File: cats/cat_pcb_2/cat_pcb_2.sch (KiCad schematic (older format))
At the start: 6 parts, among them SW1 SMT_SPDT

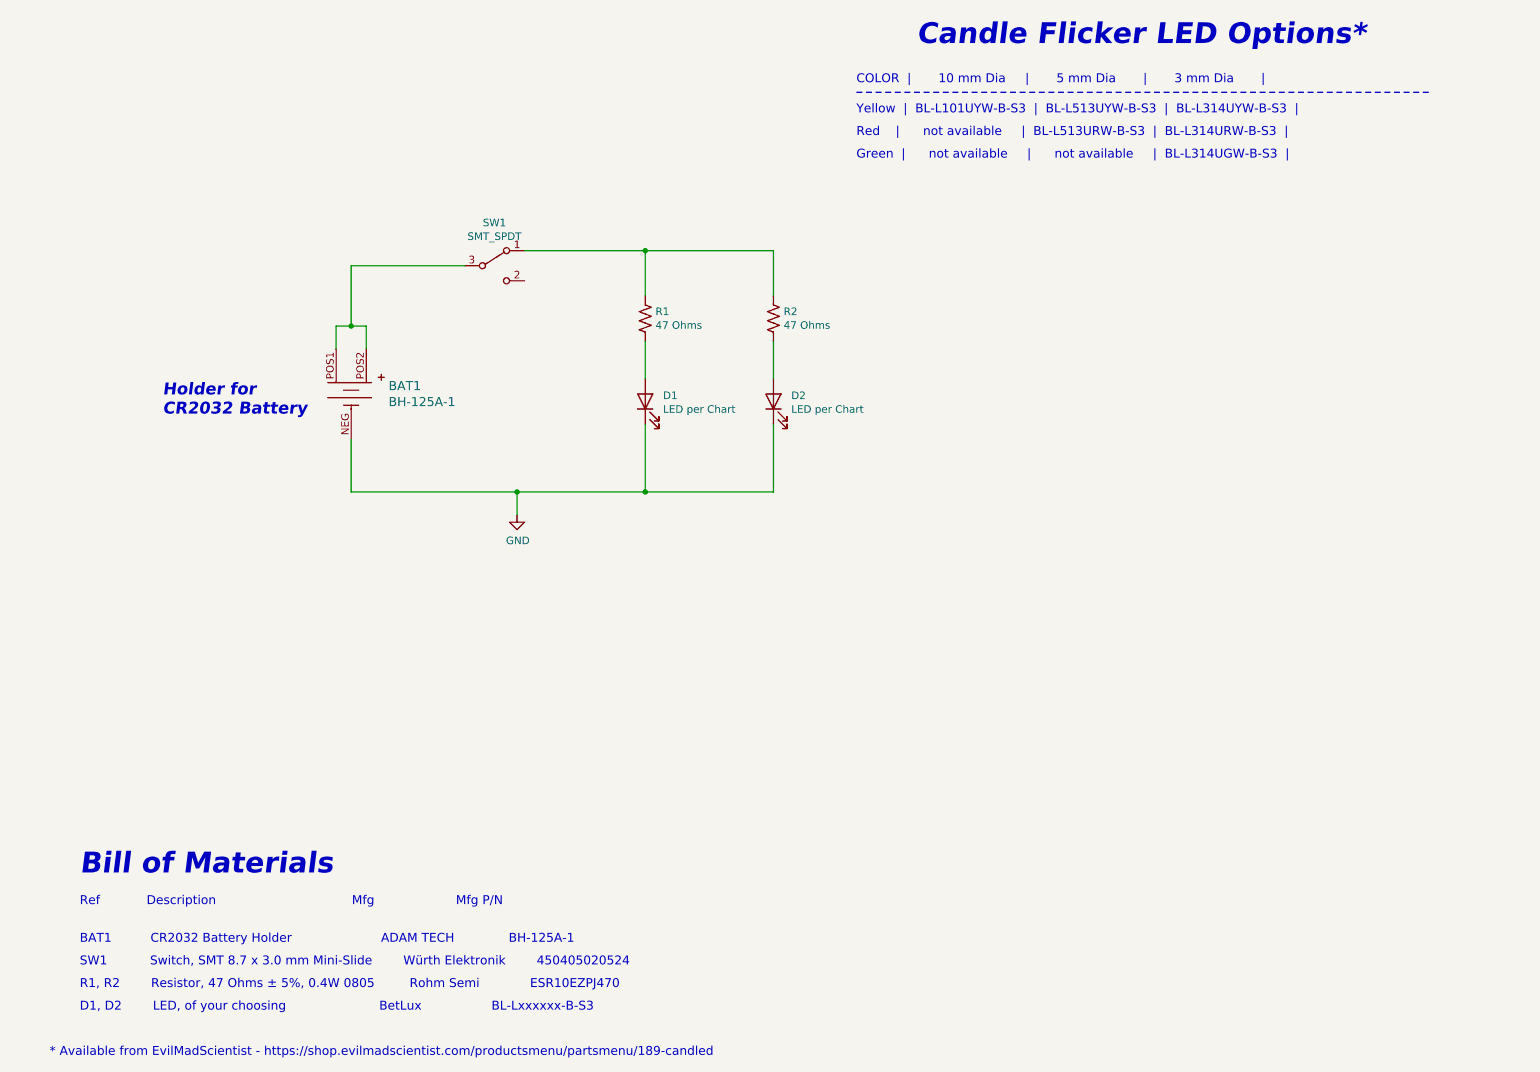
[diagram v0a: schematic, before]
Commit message: Updating all PCBS, etc.
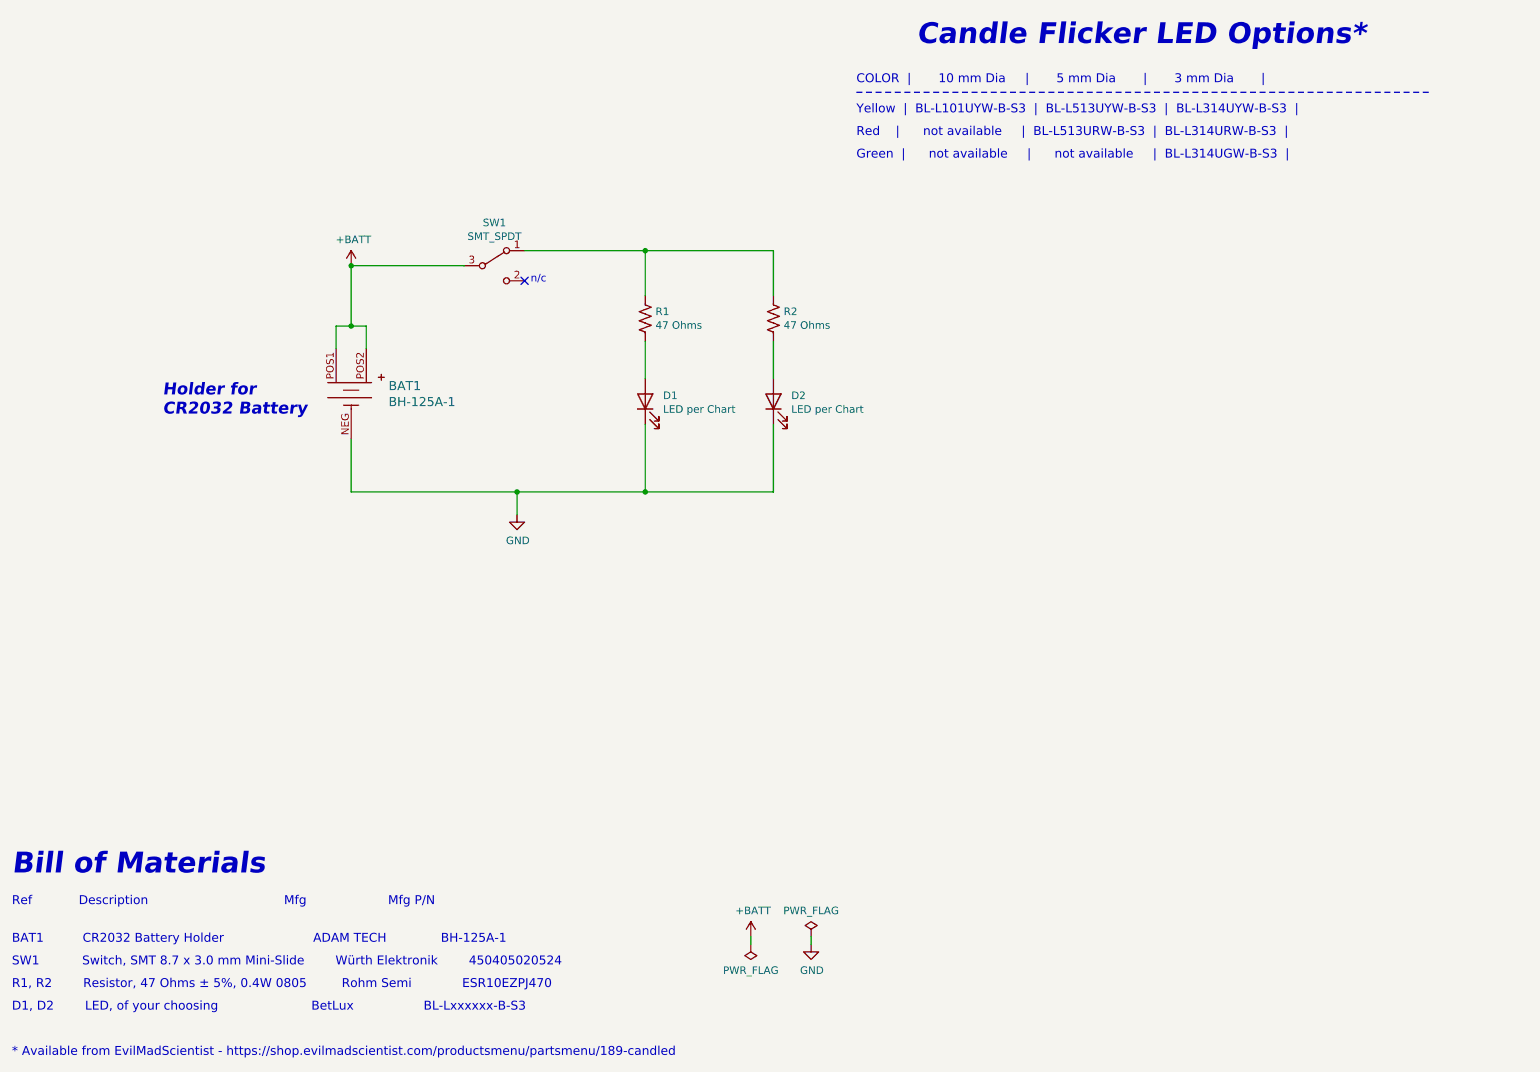
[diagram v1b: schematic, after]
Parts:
- BAT1: footprint (none) -> Battery:BatteryHolder_AdamTech_BH-125A-1
- D1, D2: footprint (none) -> LED_THT:LED_D3.0mm
- R1, R2: footprint (none) -> Resistor_SMD:R_0805_2012Metric
- SW1: footprint (none) -> Button_Switch_SMD:SMT_Mini_Slide_Switch
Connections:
- net +BATT: now reaches BAT1.POS1, BAT1.POS2, SW1.3 (B)
- no-connect marks 0 -> 1
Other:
- note added: "n/c"
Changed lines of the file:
@@
 F 0 "SW1" H 3900 2785 50  0000 C CNN
 F 1 "SMT_SPDT" H 3900 2694 50  0000 C CNN
-F 2 "" H 3900 2500 50  0001 C CNN
+F 2 "Button_Switch_SMD:SMT_Mini_Slide_Switch" H 3900 2500 50  0001 C CNN
 F 3 "" H 3900 2500 50  0001 C CNN
 	1    3900 2500
@@
 F 0 "R1" H 4968 2896 50  0000 L CNN
 F 1 "47 Ohms" H 4968 2805 50  0000 L CNN
-F 2 "" V 4940 2840 50  0001 C CNN
+F 2 "Resistor_SMD:R_0805_2012Metric" V 4940 2840 50  0001 C CNN
 F 3 "~" H 4900 2850 50  0001 C CNN
 	1    4900 2850
@@
 F 0 "D1" V 4939 3282 50  0000 R CNN
 F 1 "LED per Chart" V 4848 3282 50  0000 R CNN
-F 2 "" H 4900 3400 50  0001 C CNN
+F 2 "LED_THT:LED_D3.0mm" H 4900 3400 50  0001 C CNN
 F 3 "~" H 4900 3400 50  0001 C CNN
 	1    4900 3400
@@
 F 0 "BAT1" V 2897 3598 60  0000 L CNN
 F 1 "BH-125A-1" V 3003 3598 60  0000 L CNN
-F 2 "" H 3150 3550 60  0001 L CNN
+F 2 "Battery:BatteryHolder_AdamTech_BH-125A-1" H 3150 3550 60  0001 L CNN
 F 3 "https://app.adam-tech.com/products/download/data_sheet/197006/bh-125a-1-data-sheet.pdf" H 3150 3650 60  0001 L CNN
 F 4 "2057-BH-125A-1-ND" H 3150 3750 60  0001 L CNN "Digi-Key_PN"
@@
 Wire Wire Line
 	2950 4000 4050 4000
-Text Notes 1150 6550 0    138  Italic 28
+Text Notes 700  6550 0    138  Italic 28
 Bill of Materials
-Text Notes 1150 6750 0    59   ~ 0
+Text Notes 700  6750 0    59   ~ 0
 Ref            Description                                   Mfg                     Mfg P/N
-Text Notes 1150 7000 0    59   ~ 0
+Text Notes 700  7000 0    59   ~ 0
 BAT1          CR2032 Battery Holder                       ADAM TECH              BH-125A-1
-Text Notes 1150 7150 0    59   ~ 0
+Text Notes 700  7150 0    59   ~ 0
 SW1           Switch, SMT 8.7 x 3.0 mm Mini-Slide        Würth Elektronik        450405020524
-Text Notes 1150 7300 0    59   ~ 0
+Text Notes 700  7300 0    59   ~ 0
 R1, R2        Resistor, 47 Ohms ± 5%, 0.4W 0805         Rohm Semi             ESR10EZPJ470
-Text Notes 1150 7450 0    59   ~ 0
+Text Notes 700  7450 0    59   ~ 0
 D1, D2        LED, of your choosing                        BetLux                  BL-Lxxxxxx-B-S3
 $Comp
@@
 Text Notes 1700 3500 0    79   Italic 16
   Holder for\nCR2032 Battery
-Text Notes 950  7750 0    59   ~ 0
+Text Notes 700  7750 0    59   ~ 0
 * Available from EvilMadScientist - https://shop.evilmadscientist.com/productsmenu/partsmenu/189-candled
 $Comp
@@
 F 0 "R2" H 5818 2896 50  0000 L CNN
 F 1 "47 Ohms" H 5818 2805 50  0000 L CNN
-F 2 "" V 5790 2840 50  0001 C CNN
+F 2 "Resistor_SMD:R_0805_2012Metric" V 5790 2840 50  0001 C CNN
 F 3 "~" H 5750 2850 50  0001 C CNN
 	1    5750 2850
@@
 F 0 "D2" V 5789 3282 50  0000 R CNN
 F 1 "LED per Chart" V 5698 3282 50  0000 R CNN
-F 2 "" H 5750 3400 50  0001 C CNN
+F 2 "LED_THT:LED_D3.0mm" H 5750 3400 50  0001 C CNN
 F 3 "~" H 5750 3400 50  0001 C CNN
 	1    5750 3400
@@
 	4900 2400 5750 2400
 Connection ~ 4900 2400
+NoConn ~ 4100 2600
+Text Notes 4140 2620 0    50   ~ 0
+n/c
+$Comp
+L power:+BATT #PWR0101
+U 1 1 616CFE01
+P 2950 2500
+F 0 "#PWR0101" H 2950 2350 50  0001 C CNN
+F 1 "+BATT" H 2965 2673 50  0000 C CNN
+F 2 "" H 2950 2500 50  0001 C CNN
+F 3 "" H 2950 2500 50  0001 C CNN
+	1    2950 2500
+	1    0    0    -1
+$EndComp
+Connection ~ 2950 2500
+$Comp
+L power:PWR_FLAG #FLG0101
+U 1 1 616D0847
+P 6000 6950
+F 0 "#FLG0101" H 6000 7025 50  0001 C CNN
+F 1 "PWR_FLAG" H 6000 7123 50  0000 C CNN
+F 2 "" H 6000 6950 50  0001 C CNN
+F 3 "~" H 6000 6950 50  0001 C CNN
+	1    6000 6950
+	1    0    0    -1
+$EndComp
+$Comp
+L power:PWR_FLAG #FLG0102
+U 1 1 616D0C22
+P 5600 7000
+F 0 "#FLG0102" H 5600 7075 50  0001 C CNN
+F 1 "PWR_FLAG" H 5600 7173 50  0000 C CNN
+F 2 "" H 5600 7000 50  0001 C CNN
+F 3 "~" H 5600 7000 50  0001 C CNN
+	1    5600 7000
+	-1   0    0    1
+$EndComp
+$Comp
+L power:GND #PWR0102
+U 1 1 616D159A
+P 6000 7000
+F 0 "#PWR0102" H 6000 6750 50  0001 C CNN
+F 1 "GND" H 6005 6827 50  0000 C CNN
+F 2 "" H 6000 7000 50  0001 C CNN
+F 3 "" H 6000 7000 50  0001 C CNN
+	1    6000 7000
+	1    0    0    -1
+$EndComp
+Wire Wire Line
+	6000 6950 6000 7000
+$Comp
+L power:+BATT #PWR0103
+U 1 1 616D21D7
+P 5600 6950
+F 0 "#PWR0103" H 5600 6800 50  0001 C CNN
+F 1 "+BATT" H 5615 7123 50  0000 C CNN
+F 2 "" H 5600 6950 50  0001 C CNN
+F 3 "" H 5600 6950 50  0001 C CNN
+	1    5600 6950
+	1    0    0    -1
+$EndComp
+Wire Wire Line
+	5600 6950 5600 7000
 $EndSCHEMATC
